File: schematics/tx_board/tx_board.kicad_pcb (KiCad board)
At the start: 2 copper layers, 44 x 26 mm, 16 parts, among them U1 SI4463-C2A-GM, X2 SMA

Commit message: first complete design & routing
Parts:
- removed C0: 8p2, tx_board:C0805
- removed C1: 1u/TA, tx_board:C1206
- removed C2: 10n, tx_board:C0805
- removed C3: 1n, tx_board:C0805
- removed CM1, CM2, CM3: 9p1, tx_board:C0805
- removed CM4: 13p, tx_board:C0805
- removed JP1: PINHD-2X5_90, tx_board:2X05_90
- removed L0: 30nH, tx_board:R0805
- removed LCHOKE1: 220nH, tx_board:R0805
- removed LM1: 27nH, tx_board:R0805
- removed LM2: 22nH, tx_board:R0805
- removed LM3: 15nH, tx_board:R0805
- removed U1: SI4463-C2A-GM, tx_board:QFN50P400X400X90-20N
- removed X2: SMA, tx_board:J502-ND-142-0701-871_876
- added C301: 220p, Capacitor_SMD:C_0603_1608Metric_Pad1.05x0.95mm_HandSolder, F.Cu at (94.0, 108.5)
- added C302: 10p, Capacitor_SMD:C_0603_1608Metric_Pad1.05x0.95mm_HandSolder, F.Cu at (96.5, 107.0)
- added C303: 10n, Capacitor_SMD:C_0603_1608Metric_Pad1.05x0.95mm_HandSolder, F.Cu at (92.5, 110.0)
- added C304: 10n, Capacitor_SMD:C_0603_1608Metric_Pad1.05x0.95mm_HandSolder, F.Cu at (91.0, 113.0)
- added C305: 2n2, Capacitor_SMD:C_0603_1608Metric_Pad1.05x0.95mm_HandSolder, B.Cu at (93.4, 110.4)
- added C306: 100n, Capacitor_SMD:C_0603_1608Metric_Pad1.05x0.95mm_HandSolder, F.Cu at (100.8, 104.4)
- added C307: 10n, Capacitor_SMD:C_0603_1608Metric_Pad1.05x0.95mm_HandSolder, F.Cu at (106.6, 112.3)
- added C308: 100n, Capacitor_SMD:C_0603_1608Metric_Pad1.05x0.95mm_HandSolder, B.Cu at (95.8, 107.8)
- added C309: 100n, Capacitor_SMD:C_0603_1608Metric_Pad1.05x0.95mm_HandSolder, F.Cu at (91.0, 116.6)
- added C310: 470p, Capacitor_SMD:C_0603_1608Metric_Pad1.05x0.95mm_HandSolder, B.Cu at (104.2, 104.8)
- added C311: 22n, Capacitor_SMD:C_0603_1608Metric_Pad1.05x0.95mm_HandSolder, F.Cu at (101.5, 107.0)
- added C312: 15n, Capacitor_SMD:C_0603_1608Metric_Pad1.05x0.95mm_HandSolder, B.Cu at (108.6, 109.0)
- added C313: 1n, Capacitor_SMD:C_0603_1608Metric_Pad1.05x0.95mm_HandSolder, B.Cu at (105.8, 108.0)
- added C314: 10n, Capacitor_SMD:C_0603_1608Metric_Pad1.05x0.95mm_HandSolder, F.Cu at (104.6, 107.0)
- added C315: 100n, Capacitor_SMD:C_0603_1608Metric_Pad1.05x0.95mm_HandSolder, F.Cu at (105.5, 111.2)
- added C316: 100n, Capacitor_SMD:C_0603_1608Metric_Pad1.05x0.95mm_HandSolder, F.Cu at (105.0, 120.0)
- added C317: 22u/TA, Capacitor_Tantalum_SMD:CP_EIA-3216-18_Kemet-A_Pad1.58x1.35mm_HandSolder, F.Cu at (93.2, 106.2)
- added C318: 10n, Capacitor_SMD:C_0603_1608Metric_Pad1.05x0.95mm_HandSolder, F.Cu at (106.2, 118.8)
- added C319: 6p8, Capacitor_SMD:C_0603_1608Metric_Pad1.05x0.95mm_HandSolder, F.Cu at (93.5, 104.0)
- added C320: 1000p, Capacitor_SMD:C_0603_1608Metric_Pad1.05x0.95mm_HandSolder, F.Cu at (90.0, 102.5)
- added C321: 9p1, Capacitor_SMD:C_0603_1608Metric_Pad1.05x0.95mm_HandSolder, F.Cu at (87.5, 105.0)
- added C322: 9p1, Capacitor_SMD:C_0603_1608Metric_Pad1.05x0.95mm_HandSolder, F.Cu at (85.5, 105.0)
- added G***: LOGO, lib:m17_silk_Logo, B.Cu at (113.6, 98.9)
- added G***: LOGO, lib:m17_silk_Logo, F.Cu at (113.5, 99.1)
- added J1: Conn_02x14_Odd_Even, Connector_PinHeader_2.54mm:PinHeader_2x14_P2.54mm_Horizontal, F.Cu at (118.2, 127.0)
- added J301: Out, Connector_Coaxial:SMA_Samtec_SMA-J-P-X-ST-EM1_EdgeMount, F.Cu at (82.0, 102.5)
- added L301: 15n, Inductor_SMD:L_0603_1608Metric_Pad1.05x0.95mm_HandSolder, F.Cu at (98.5, 107.0)
- added L302: DNP, Inductor_SMD:L_0603_1608Metric_Pad1.05x0.95mm_HandSolder, F.Cu at (103.0, 107.0)
- added L303: 20n, Inductor_SMD:L_0603_1608Metric_Pad1.05x0.95mm_HandSolder, F.Cu at (96.5, 103.5)
- added L304: 22n, Inductor_SMD:L_0603_1608Metric_Pad1.05x0.95mm_HandSolder, F.Cu at (93.5, 102.5)
- added L305: 15nH, Inductor_SMD:L_0603_1608Metric_Pad1.05x0.95mm_HandSolder, F.Cu at (86.5, 102.5)
- added R301: 22k, Resistor_SMD:R_0603_1608Metric_Pad1.05x0.95mm_HandSolder, B.Cu at (91.6, 110.4)
- added R302: 1k1, Resistor_SMD:R_0603_1608Metric_Pad1.05x0.95mm_HandSolder, F.Cu at (92.5, 111.5)
- added R303: 47k, Resistor_SMD:R_0603_1608Metric_Pad1.05x0.95mm_HandSolder, B.Cu at (92.4, 107.8)
- added R304: 3k6, Resistor_SMD:R_0603_1608Metric_Pad1.05x0.95mm_HandSolder, F.Cu at (91.0, 115.2)
- added R305: 3R9, Resistor_SMD:R_0603_1608Metric_Pad1.05x0.95mm_HandSolder, F.Cu at (100.0, 107.0)
- added R306: 47k, Resistor_SMD:R_0603_1608Metric_Pad1.05x0.95mm_HandSolder, B.Cu at (99.2, 107.8)
- added R307: 100, Resistor_SMD:R_0603_1608Metric_Pad1.05x0.95mm_HandSolder, B.Cu at (102.4, 108.0)
- added R308: 560, Resistor_SMD:R_0603_1608Metric_Pad1.05x0.95mm_HandSolder, B.Cu at (104.2, 106.4)
- added R309: 270, Resistor_SMD:R_0603_1608Metric_Pad1.05x0.95mm_HandSolder, B.Cu at (107.6, 106.4)
- added REF**: OSHW-Logo2_7.3x6mm_SilkScreen, Symbol:OSHW-Logo2_7.3x6mm_SilkScreen, B.Cu at (115.0, 105.0)
- added RN301: 4 x 1k ISOLATED, Resistor_SMD:R_Array_Concave_4x0603, F.Cu at (102.5, 122.0)
- added RN302: 4 x 1k ISOLATED, Resistor_SMD:R_Array_Concave_4x0603, F.Cu at (110.4, 122.0)
- added TP301: TestPoint_Probe, TestPoint:TestPoint_Pad_D1.0mm, B.Cu at (101.2, 102.0)
- added TP302: TestPoint_Probe, TestPoint:TestPoint_Pad_D1.0mm, B.Cu at (103.8, 102.0)
- added TP303: TestPoint_Probe, TestPoint:TestPoint_Pad_D1.0mm, B.Cu at (106.6, 102.0)
- added U301: ADF7021, Package_CSP:LFCSP-48-1EP_7x7mm_P0.5mm_EP4.1x4.1mm_ThermalVias, F.Cu at (100.0, 115.0)
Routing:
- net +3V3: track 35.9 -> 133.2 mm, vias 1 -> 9
- net GND: track 2.94 -> 58.4 mm, vias 77 -> 75
- net FM_MOD: track 0.00 -> 27.4 mm
- net EXT_OSC2_IN: track 0.00 -> 19.2 mm
- net ADF_SWD: track 0.00 -> 18.7 mm
- net Net-(C313-Pad1): track 0.00 -> 13.9 mm, vias 0 -> 1
- net /SCLK: track 12.7 -> 0.00 mm
- net Net-(R306-Pad1): track 0.00 -> 11.1 mm, vias 0 -> 1
- net /NIRQ: track 11.1 -> 0.00 mm
- net Net-(RN302-Pad1): track 0.00 -> 10.4 mm
- net /SDI: track 9.71 -> 0.00 mm
- net Net-(RN302-Pad2): track 0.00 -> 9.22 mm
- net Net-(RN302-Pad3): track 0.00 -> 8.72 mm
- net Net-(CM3-Pad1): track 8.63 -> 0.00 mm
- net ADF_SLE: track 0.00 -> 8.37 mm
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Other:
- board size 44 x 26 mm -> 40 x 38.6 mm
- rule pad_to_mask_clearance: 0.051 -> 0
- board text added: "Repeater TX Board"
- board text removed: "REP_TX_BOARD_1.0"

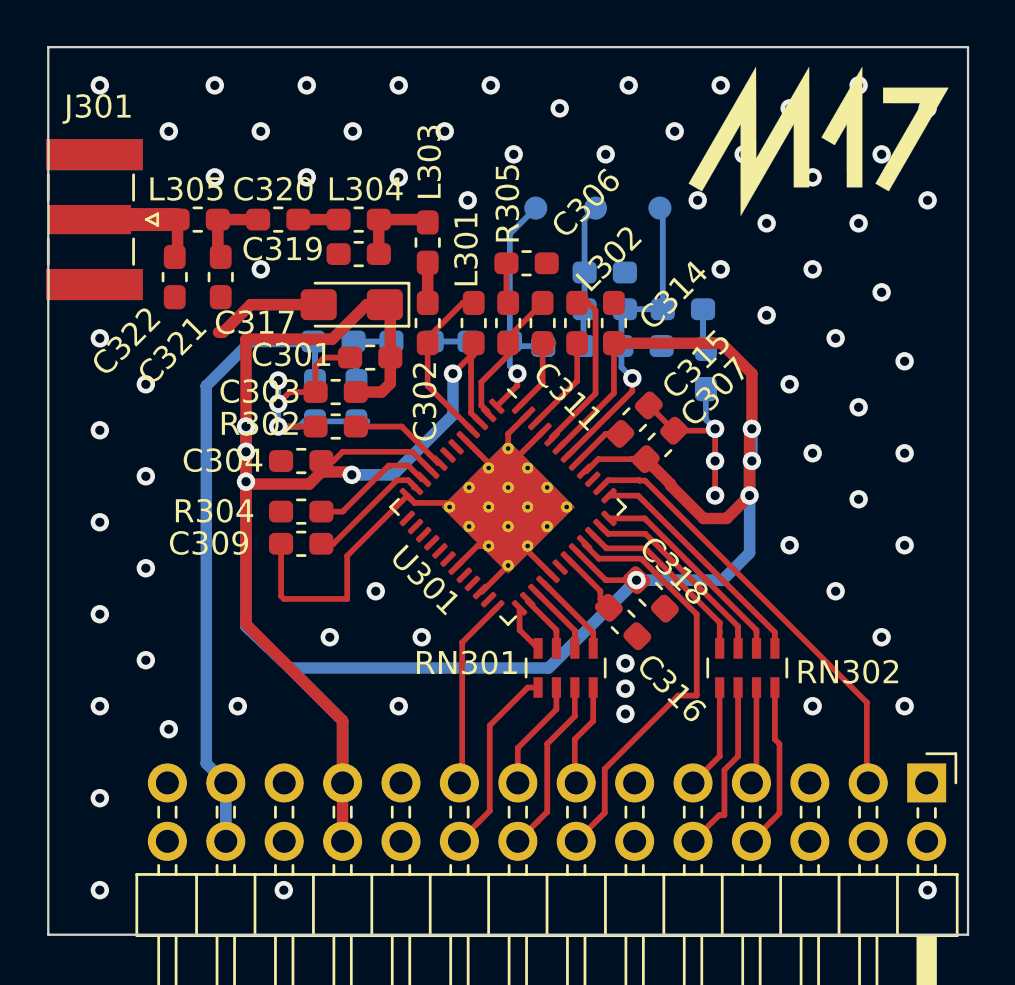
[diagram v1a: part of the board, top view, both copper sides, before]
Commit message: Silk mask cleaning, better decoupling
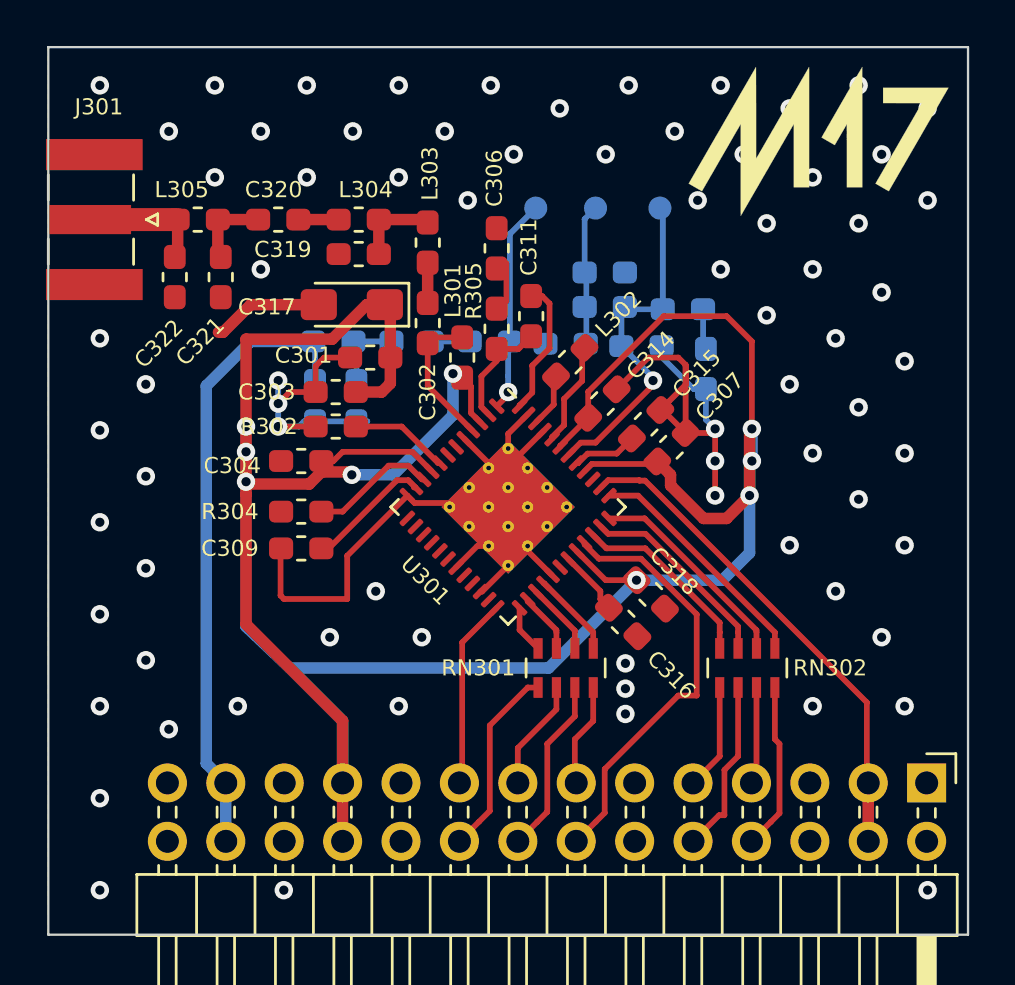
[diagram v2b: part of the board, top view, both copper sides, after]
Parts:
- moved C314 3.54 mm to (104.1, 110.5), turned to 45 degrees
- moved L302 1.73 mm to (102.7, 108.7), turned to 45 degrees
- moved L301 1.58 mm to (98.0, 108.5)
- moved C306 1.45 mm to (99.5, 103.8), turned to 90 degrees
- moved C311 0.58 mm to (101.0, 106.7), turned to 270 degrees
- moved R305 0.56 mm to (99.5, 107.2)
- moved C315 0.54 mm to (106.0, 111.4)
- moved C307 0.51 mm to (107.1, 112.4)
- moved C309 0.20 mm to (91.0, 116.8)
- moved R307 0.14 mm to (102.5, 107.9)
- moved R308 0.10 mm to (104.2, 106.3)
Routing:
- net GND: track 58.4 -> 69.8 mm
- net Net-(L302-Pad2): track 7.30 -> 4.19 mm
- net EXT_OSC2_IN: track 19.2 -> 21.8 mm
- net Net-(C311-Pad1): track 3.63 -> 5.94 mm
- net Net-(L302-Pad1): track 4.19 -> 2.03 mm
- net +3V3: track 133.2 -> 131.6 mm
- net Net-(C302-Pad2): track 7.46 -> 6.21 mm
- net Net-(C313-Pad1): track 13.9 -> 15.0 mm
- net Net-(C311-Pad2): track 6.08 -> 4.98 mm

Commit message: shielded version
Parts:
- removed the G*** at (113.6, 98.9)
- removed the G*** at (113.5, 99.1)
- removed the REF** at (115.0, 105.0)
- added G***: LOGO, lib:m17_silk_Logo, B.Cu at (160.2, 120.0)
- added G***: LOGO, lib:m17_silk_Logo, F.Cu at (133.3, 114.1)
- added G***: LOGO, lib:Ham_Logo, F.Cu at (189.3, 65.6)
- added H1: Würt_LGA_Shielding, lib:WE_36103205_SMD, F.Cu at (147.2, 107.9)
- added REF**: OSHW-Logo2_9.8x8mm_SilkScreen, Symbol:OSHW-Logo2_9.8x8mm_SilkScreen, B.Cu at (135.3, 115.7)
- added REF**: OSHW-Logo2_9.8x8mm_SilkScreen, Symbol:OSHW-Logo2_9.8x8mm_SilkScreen, F.Cu at (161.5, 98.0)
- added REF**: ESD-Logo_6.6x6mm_SilkScreen, Symbol:ESD-Logo_6.6x6mm_SilkScreen, F.Cu at (156.5, 73.3)
- C306, C307, C311, C314, C315, C316, C317, C318, R302, R305: moved to B.Cu
- J1: footprint Connector_PinHeader_2.54mm:PinHeader_2x14_P2.54mm_Horizontal -> edge_contact:edge_2x14pin
- moved R301 68.0 mm to (158.8, 99.5), turned to 180 degrees
- moved R303 65.3 mm to (156.9, 98.0), turned to 180 degrees
- moved TP301 60.8 mm to (162.0, 100.7), turned to 180 degrees
- moved C305 60.0 mm to (152.2, 98.0), turned to 0 degrees
- moved C308 59.4 mm to (154.6, 98.9), turned to 90 degrees
- moved TP302 58.2 mm to (162.0, 104.0), turned to 180 degrees
- moved C304 57.7 mm to (147.7, 102.4)
- moved R302 57.3 mm to (149.5, 105.3), turned to 270 degrees
- moved R306 57.3 mm to (156.1, 100.7), turned to 90 degrees
- moved C303 56.2 mm to (147.2, 96.9), turned to 90 degrees
- moved TP303 55.6 mm to (162.0, 106.8), turned to 180 degrees
- moved C309 54.5 mm to (144.2, 105.0)
- moved R304 54.5 mm to (144.2, 103.5)
- moved C310 53.6 mm to (157.8, 102.6), turned to 90 degrees
- moved R307 53.6 mm to (156.0, 104.0), turned to 90 degrees
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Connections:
- J1 pad 1: GND -> ADF_CE
- J1 pad 10: SPI2_MISO -> GND
- J1 pad 11: GND -> ADF_SWD
- J1 pad 12: GND -> ADF_SWD
- J1 pad 13: ADF_SCLK -> SPI2_MOSI
- J1 pad 14: ADF_SWD -> SPI2_MOSI
- J1 pad 15: ADF_SDATA -> SPI2_MISO
- J1 pad 16: ADF_SREAD -> SPI2_MISO
- J1 pad 17: ADF_CE -> SPI2_SCK
- J1 pad 18: ADF_SLE -> SPI2_SCK
- J1 pad 19: GND -> ADF_MUXOUT
- J1 pad 20: GND -> ADF_MUXOUT
- J1 pad 21: +3V3 -> GND
- J1 pad 22: +3V3 -> GND
- J1 pad 23: GND -> EXT_OSC2_IN
- J1 pad 24: GND -> EXT_OSC2_IN
- J1 pad 25: FM_MOD -> GND
- J1 pad 26: FM_MOD -> GND
- J1 pad 27: GND -> FM_MOD
- J1 pad 28: GND -> FM_MOD
- J1 pad 3: EXT_OSC2_IN -> ADF_SLE
- J1 pad 4: EXT_OSC2_IN -> +3V3
- J1 pad 5: GND -> ADF_SDATA
- J1 pad 7: SPI2_SCK -> ADF_SREAD
- J1 pad 8: ADF_MUXOUT -> +3V3
- J1 pad 9: SPI2_MOSI -> ADF_SCLK
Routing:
- net +3V3: track 131.6 -> 86.3 mm, vias 9 -> 11
- net ADF_CE: track 8.29 -> 27.3 mm
- net GND: track 69.8 -> 88.8 mm, vias 75 -> 87
- net ADF_SDATA: track 4.85 -> 19.4 mm
- net ADF_SLE: track 8.37 -> 21.3 mm
- net ADF_SCLK: track 4.51 -> 15.4 mm
- net SPI2_MOSI: track 4.63 -> 14.9 mm, vias 0 -> 2
- net ADF_SREAD: track 7.72 -> 17.6 mm
- net FM_MOD: track 27.4 -> 36.5 mm, vias 0 -> 2
- net SPI2_SCK: track 4.24 -> 12.2 mm, vias 0 -> 2
- net Net-(RN302-Pad1): track 10.4 -> 4.24 mm
- net Net-(RN302-Pad2): track 9.22 -> 3.50 mm
- net Net-(RN302-Pad3): track 8.72 -> 3.33 mm
- net SPI2_MISO: track 7.64 -> 12.9 mm, vias 0 -> 2
- net Net-(RN302-Pad4): track 8.23 -> 3.52 mm
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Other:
- board size 40 x 38.6 mm -> 36 x 37 mm
- copper layers 2 -> 4
- board text added: "2m/70cm Digital Repeater TX"
- board text added: "DB9MAT Mathis SO3ALG Nikoloz SP5WWP Wojciech"
- board text removed: "Repeater TX Board"

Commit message: PA boad smd version, 50Ohms microstrip
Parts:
- removed the G*** at (189.3, 65.6)
- removed the REF** at (156.5, 73.3)
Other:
- board text added: "2m 70cm"
